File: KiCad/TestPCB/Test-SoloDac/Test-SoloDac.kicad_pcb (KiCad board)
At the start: 2 copper layers, 26 parts, among them J1 Conn_01x01_Male, J2 Conn_01x01_Male, U1 TL431D

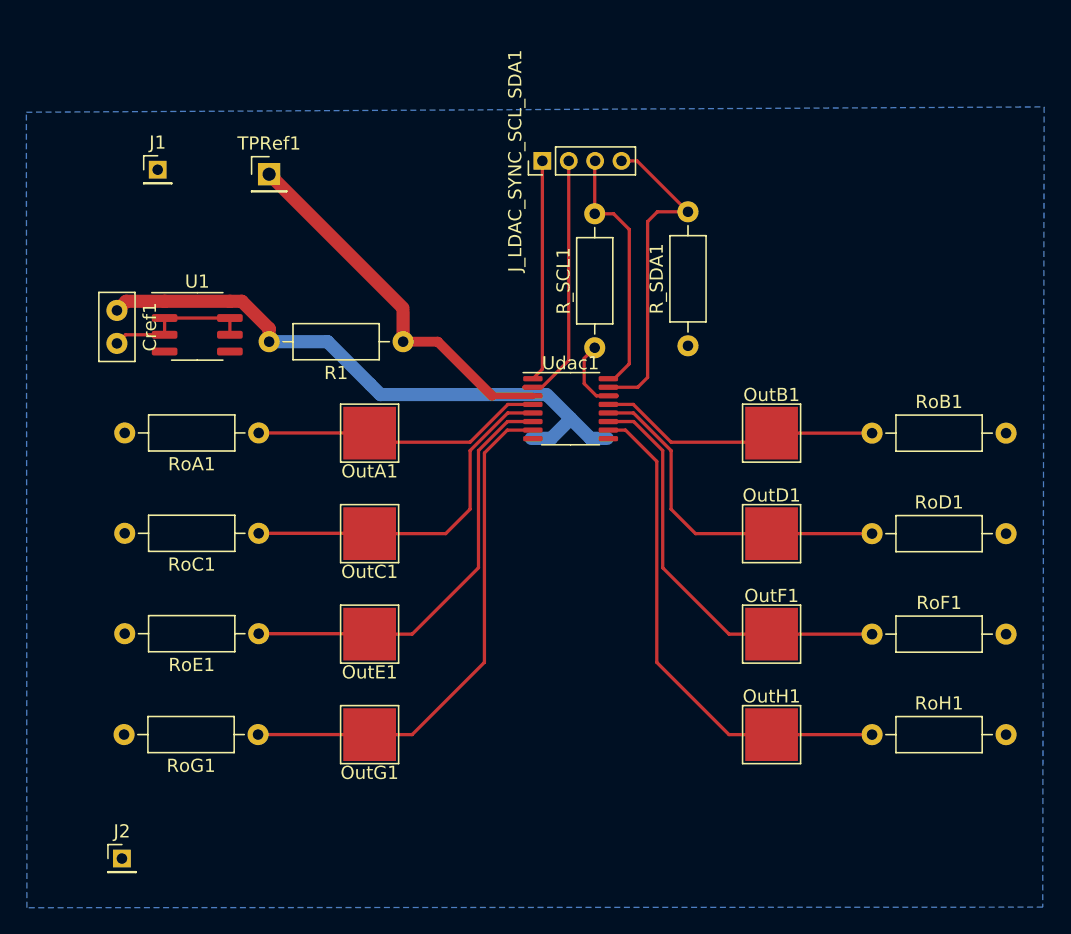
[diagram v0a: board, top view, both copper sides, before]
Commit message: Removidos los pads. Agregados pines y jumpers
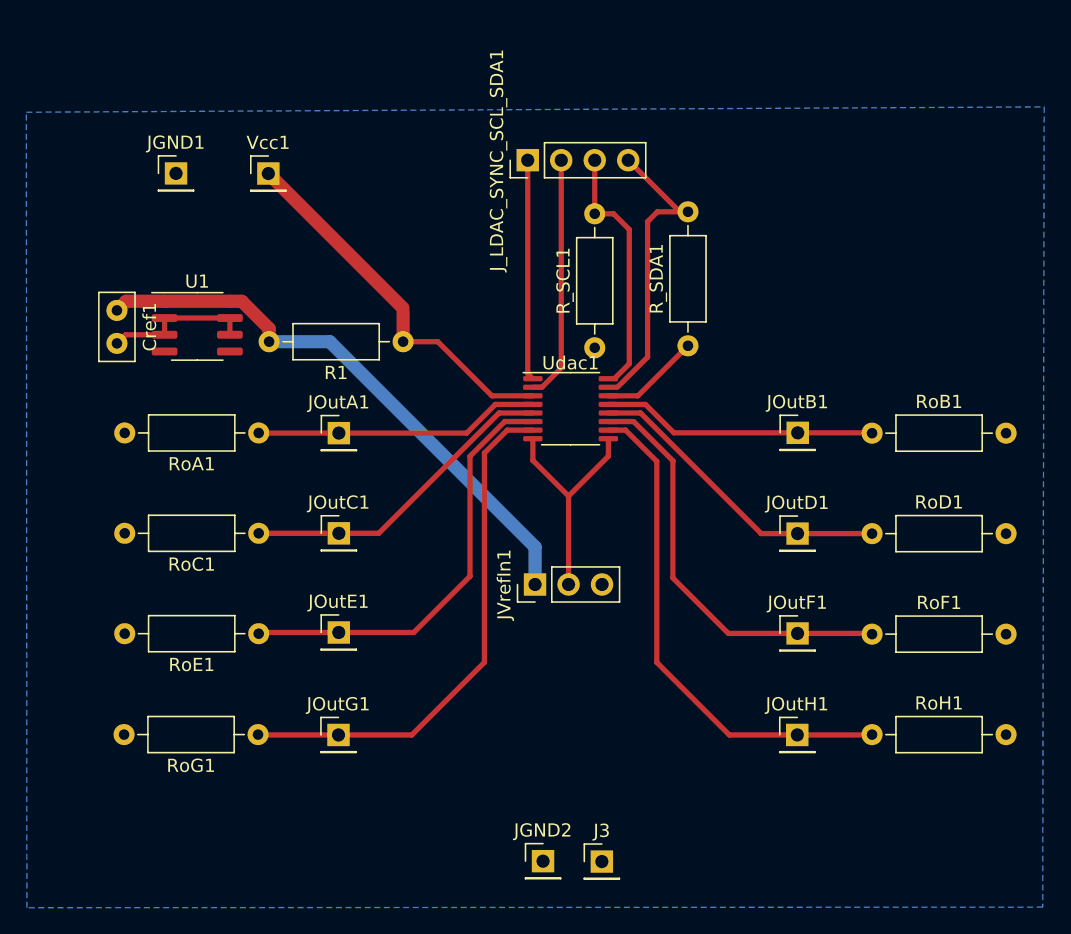
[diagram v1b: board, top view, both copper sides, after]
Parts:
- removed OutA1, OutB1, OutC1, OutD1, OutE1, OutF1, OutG1, OutH1: TestPoint, TestPoint:TestPoint_Pad_4.0x4.0mm
- added J3: Conn_01x01_Male, Connector_PinHeader_2.54mm:PinHeader_1x01_P2.54mm_Vertical, F.Cu at (63.3, 123.2)
- added JOutA1: Conn_01x01_Male, Connector_PinHeader_2.54mm:PinHeader_1x01_P2.54mm_Vertical, F.Cu at (43.4, 90.8)
- added JOutB1: Conn_01x01_Male, Connector_PinHeader_2.54mm:PinHeader_1x01_P2.54mm_Vertical, F.Cu at (78.2, 90.7)
- added JOutC1: Conn_01x01_Male, Connector_PinHeader_2.54mm:PinHeader_1x01_P2.54mm_Vertical, F.Cu at (43.4, 98.3)
- added JOutD1: Conn_01x01_Male, Connector_PinHeader_2.54mm:PinHeader_1x01_P2.54mm_Vertical, F.Cu at (78.2, 98.4)
- added JOutE1: Conn_01x01_Male, Connector_PinHeader_2.54mm:PinHeader_1x01_P2.54mm_Vertical, F.Cu at (43.4, 105.9)
- added JOutF1: Conn_01x01_Male, Connector_PinHeader_2.54mm:PinHeader_1x01_P2.54mm_Vertical, F.Cu at (78.2, 105.9)
- added JOutG1: Conn_01x01_Male, Connector_PinHeader_2.54mm:PinHeader_1x01_P2.54mm_Vertical, F.Cu at (43.4, 113.6)
- added JOutH1: Conn_01x01_Male, Connector_PinHeader_2.54mm:PinHeader_1x01_P2.54mm_Vertical, F.Cu at (78.2, 113.6)
- added JVrefIn1: Jumper_3_Open, Connector_PinHeader_2.54mm:PinHeader_1x03_P2.54mm_Vertical, F.Cu at (58.3, 102.2)
- JGND1: renamed from J1; footprint Connector_PinHeader_2.00mm:PinHeader_1x01_P2.00mm_Vertical -> Connector_PinHeader_2.54mm:PinHeader_1x01_P2.54mm_Vertical
- JGND2: renamed from J2; footprint Connector_PinHeader_2.00mm:PinHeader_1x01_P2.00mm_Vertical -> Connector_PinHeader_2.54mm:PinHeader_1x01_P2.54mm_Vertical
- J_LDAC_SYNC_SCL_SDA1: footprint Connector_PinHeader_2.00mm:PinHeader_1x04_P2.00mm_Vertical -> Connector_PinHeader_2.54mm:PinHeader_1x04_P2.54mm_Vertical
- moved JGND2 31.9 mm to (58.9, 123.2)
- moved JGND1 1.42 mm to (31.0, 71.1)
- moved J_LDAC_SYNC_SCL_SDA1 1.11 mm to (57.7, 70.1)
- moved Vcc1 0.08 mm to (38.0, 71.1)
- renumbered TPRef1 to Vcc1
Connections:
- net Net-(OutE1-Pad1) renamed VoutE
- net Net-(OutF1-Pad1) renamed VoutF
- net Net-(OutG1-Pad1) renamed VoutG
- Cref1 pad 1: Net-(Udac1-Pad8) -> Net-(Cref1-Pad1)
- R1 pad 2: Net-(Udac1-Pad8) -> Net-(Cref1-Pad1)
- U1 pad 1: Net-(Udac1-Pad8) -> Net-(Cref1-Pad1)
- U1 pad 8: Net-(Udac1-Pad8) -> Net-(Cref1-Pad1)
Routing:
- net Net-(Cref1-Pad1): track 0.00 -> 43.1 mm
- net Net-(Udac1-Pad8): track 46.1 -> 17.8 mm
- net VoutC: track 27.2 -> 24.6 mm
- net VoutD: track 26.4 -> 23.8 mm
- net Net-(J_LDAC_SYNC_SCL_SDA1-Pad4): track 25.3 -> 23.0 mm
- net GND: track 17.3 -> 19.0 mm
- net VoutA: track 22.9 -> 21.7 mm
- net VoutB: track 22.2 -> 20.9 mm
- net Net-(J_LDAC_SYNC_SCL_SDA1-Pad2): track 19.4 -> 18.5 mm

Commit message: Pistas mas gruesas. Pista para 3,3V
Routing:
- net +3V3: track 0.00 -> 42.0 mm
- net GND: track 19.0 -> 29.4 mm
- net VoutC: track 24.6 -> 25.4 mm
- net VoutD: track 23.8 -> 24.6 mm
- net VoutF: track 31.9 -> 32.4 mm
